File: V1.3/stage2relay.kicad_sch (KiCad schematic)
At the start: 5 parts, among them SW2 SW_Push

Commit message: clarify door-activator role || Active & Passive door operation
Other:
- note added: "Connection to mains-fused-H/L1 ==> Regulated by two controllers in logical 'OR' configuration - bypass key (manual activation) - S1-1 'set' relay for SW 'enable'"
- note removed: "Switched by bypass or microcontroller and Stage 1-1 relay"
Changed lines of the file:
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@@
     (stroke (width 0) (type default) (color 0 0 0 0))
   )
-  (text "Switched by bypass\nor microcontroller\nand Stage 1-1 relay"
-    (at 53.34 97.79 0)
-    (effects (font (size 1.27 1.27)) (justify right bottom))
+  (text "Connection to mains-fused-H/L1\n==> Regulated by two controllers \n      in logical 'OR' configuration\n    - bypass key (manual activation)\n    - S1-1 'set' relay for SW 'enable'"
+    (at 26.67 102.87 0)
+    (effects (font (size 1.27 1.27)) (justify left bottom))
   )
   (text "The previous Tool-Controller design was almost this section of the circuit (with simpler Microcontroller connection)."

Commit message: update v1.3 schematic documentation
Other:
- note added: "The previous Tool-Controller design was just this section of the circuit (with simpler Microcontroller connection)."
- note removed: "The previous Tool-Controller design was almost this section of the circuit (with simpler Microcontroller connection)."
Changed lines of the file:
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@@
     (effects (font (size 1.27 1.27)) (justify left bottom))
   )
-  (text "The previous Tool-Controller design was almost this section of the circuit (with simpler Microcontroller connection)."
+  (text "The previous Tool-Controller design was just this section of the circuit (with simpler Microcontroller connection)."
     (at 21.59 48.26 0)
-    (effects (font (size 1.27 1.27)) (justify left bottom))
+    (effects (font (size 1.5 1.5)) (justify left bottom))
   )
   (text "Mains power needs connected here, and will power the whole box.\nExcept, perhaps, the tool. If more exotic power is needed.\n\nLabeled on PCB as H/L1 & N/L2 to cover the bases (that both may be live)."
@@
   (text "If there is a Stage 3 relay, then Stage 2 relay can have a lowered switching current -> down to approximately 2amps"
     (at 21.59 38.1 0)
-    (effects (font (size 1.27 1.27)) (justify left bottom))
+    (effects (font (size 1.5 1.5)) (justify left bottom))
   )
   (text "The E-Stop light runs at 5V, and is shown here\nbecuase it conceptually makes sense on the sheet.\n\nThis lamp-to-switch connection is done on the \nmodular E-Stop switches themselves, not any PCB. \n\nThe middle 'read-E-stop' informs the microcontroller."
@@
   (text "active self-latching of a relay   https://electronics.stackexchange.com/questions/223691/self-latching-relay"
     (at 21.59 30.48 0)
-    (effects (font (size 1.27 1.27)) (justify left bottom))
+    (effects (font (size 1.5 1.5)) (justify left bottom))
   )
   (text "Fuse Protected Power Inputs" (at 175.26 137.16 0)
@@
   (text "Provides the majority of the Member's interface experience\n"
     (at 21.59 43.18 0)
-    (effects (font (size 1.27 1.27)) (justify left bottom))
+    (effects (font (size 1.5 1.5)) (justify left bottom))
   )
   (text "This portion of the circuit allows the Stage 2 Relay to turn on & stay on.\nWhen enabled [by ESP32 or Bypass] a person can turn on the relay with the green button.\nOnce activated, the link from relay pin 5_to_13 'latch' the relay on while powered, until reset.\nThe \"Can-Turn-On\" light will shine if it is possible to 'set' the relay for any reason.\nThe light is important, because it shows a working system or if bypass mode is enabled by a key."

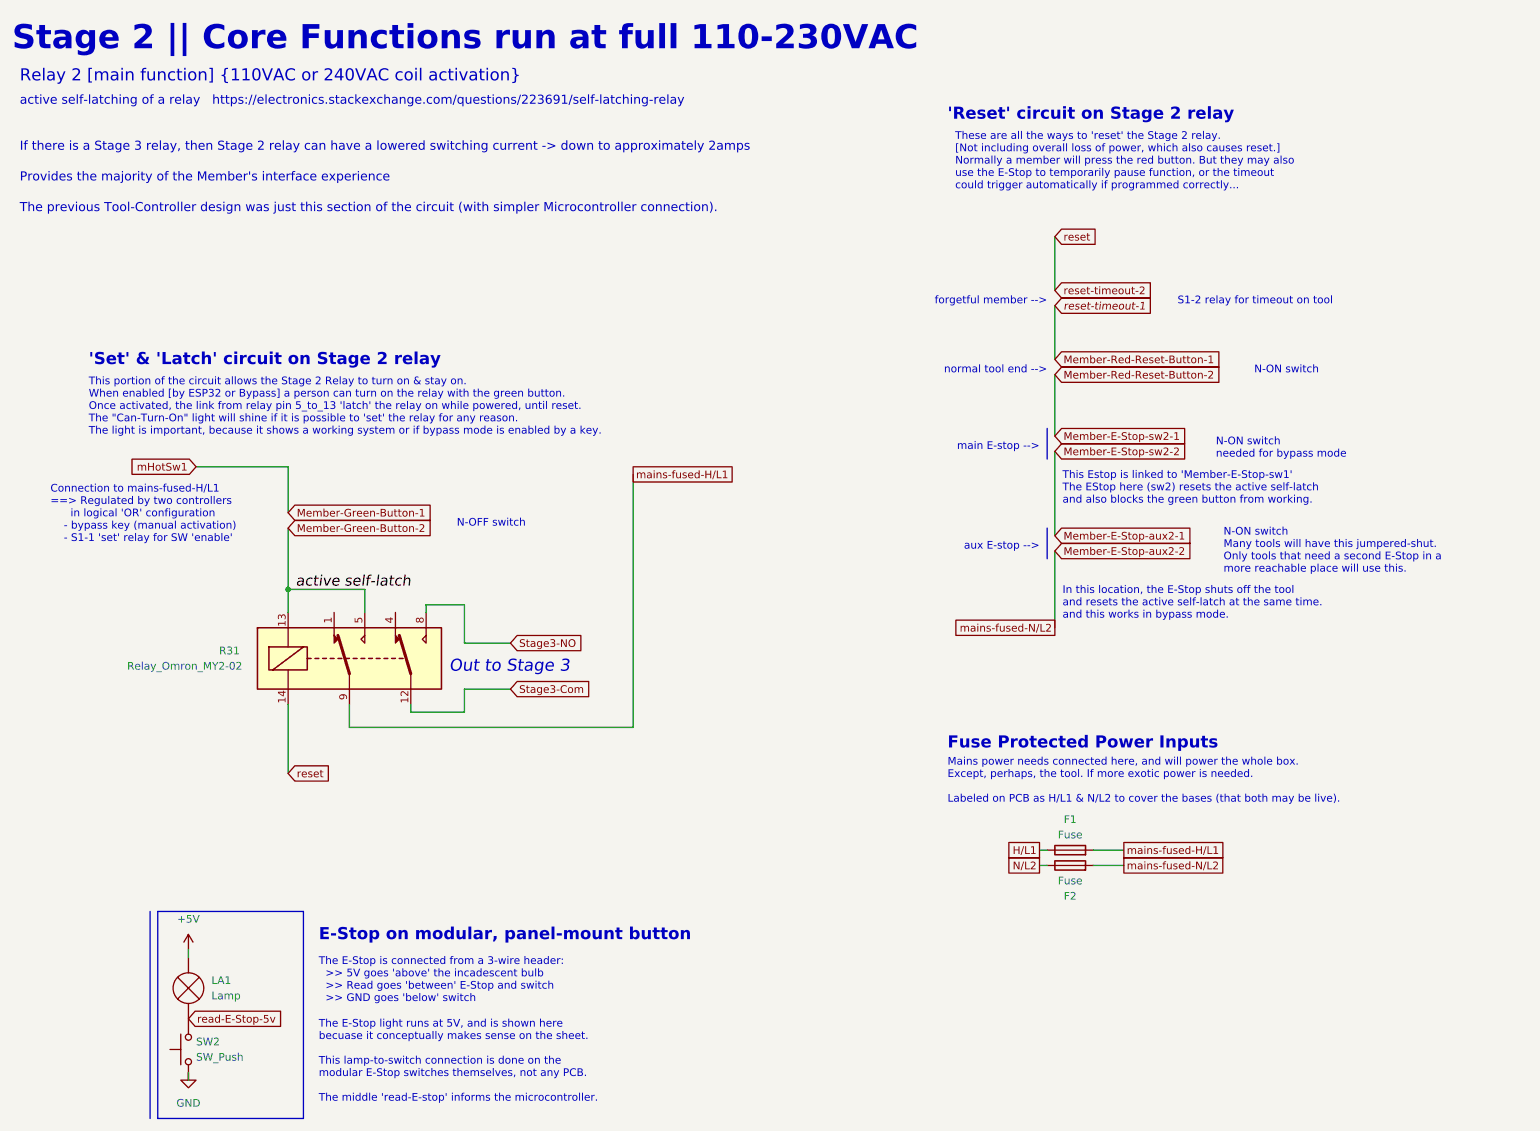
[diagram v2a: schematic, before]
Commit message: started adding the feather footprint to the board. need to update board shape and silkscreens
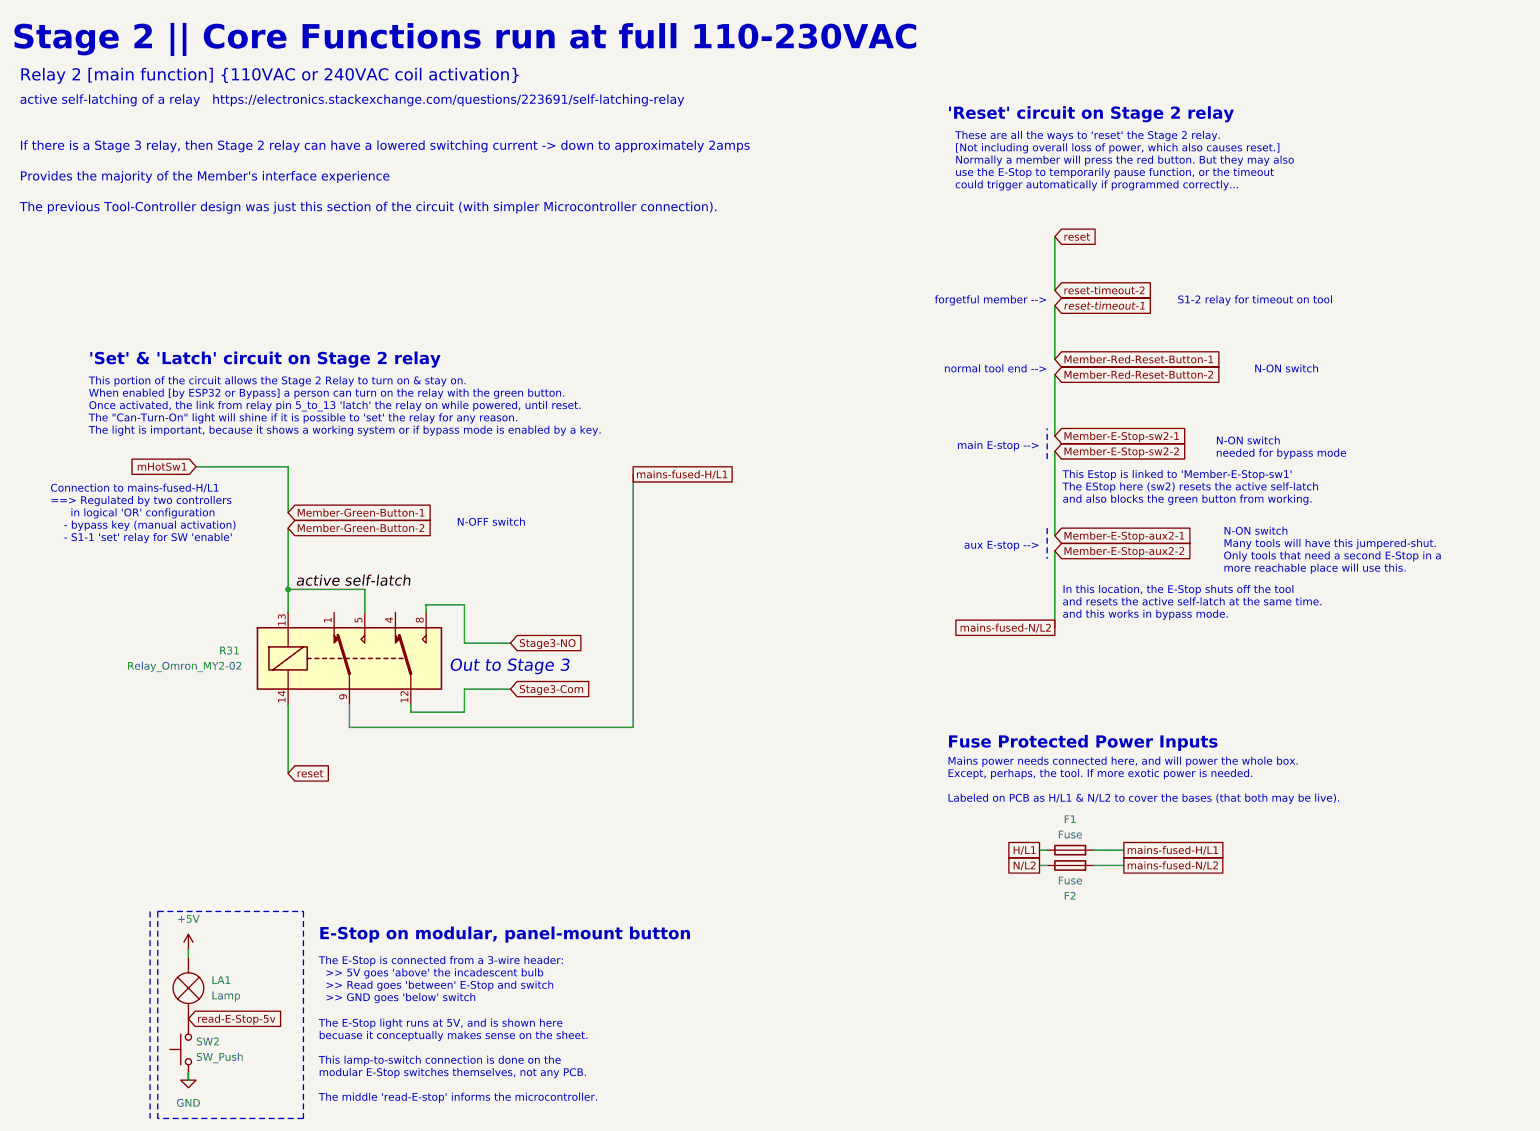
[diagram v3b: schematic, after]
